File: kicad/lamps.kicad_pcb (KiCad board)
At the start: 2 copper layers, 30.5 x 31.8 mm, 24 parts, among them J1 BARREL_JACK, J2 Screw_Terminal_1x04, J3 Screw_Terminal_1x04, J4 CONN_01X05, Q1 NMOS-PMOS-SOT23-6, Q2 NMOS-PMOS-SOT23-6, Q3 NMOS-PMOS-SOT23-6, Q4 NMOS-PMOS-SOT23-6, Q5 NMOS-PMOS-SOT23-6, Q6 NMOS-PMOS-SOT23-6, U1 ESP-12E, U2 LD1117S33CTR

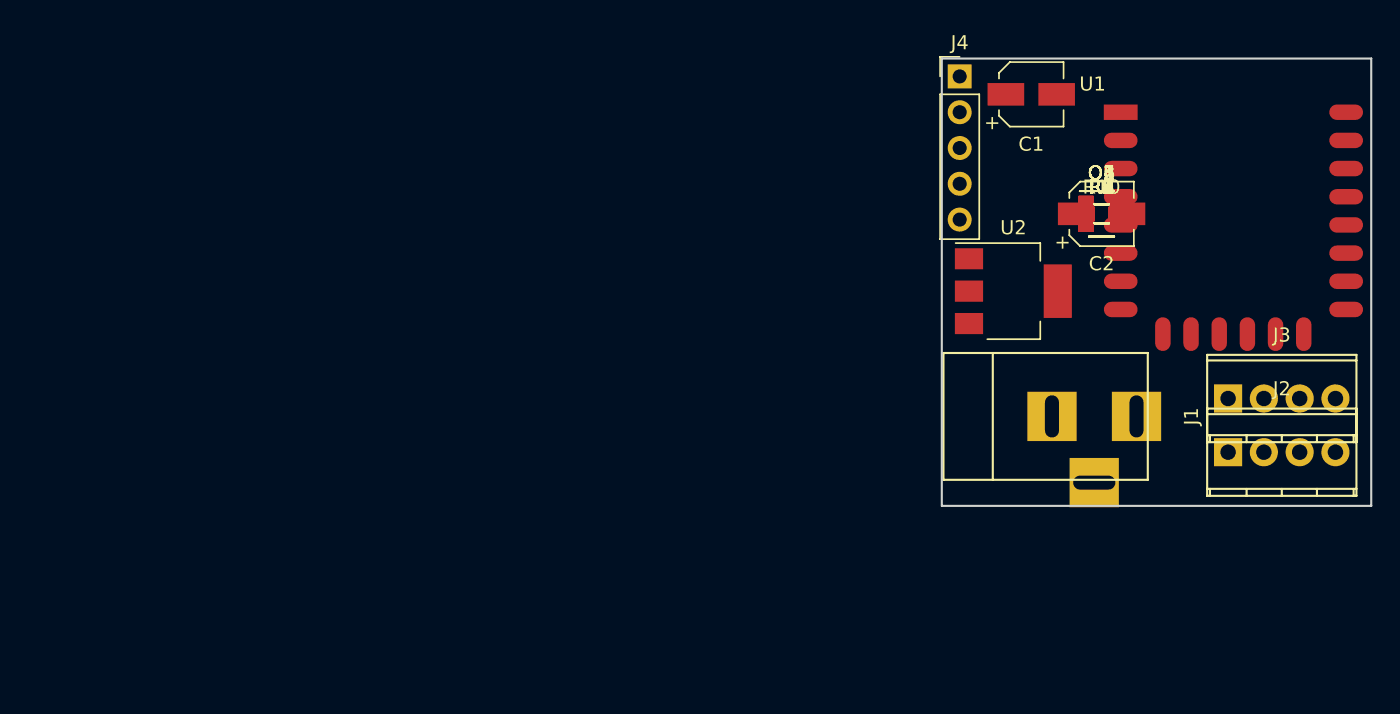
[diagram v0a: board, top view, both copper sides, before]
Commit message: start the pcb - the current layout pdf is definitely not the way Im going
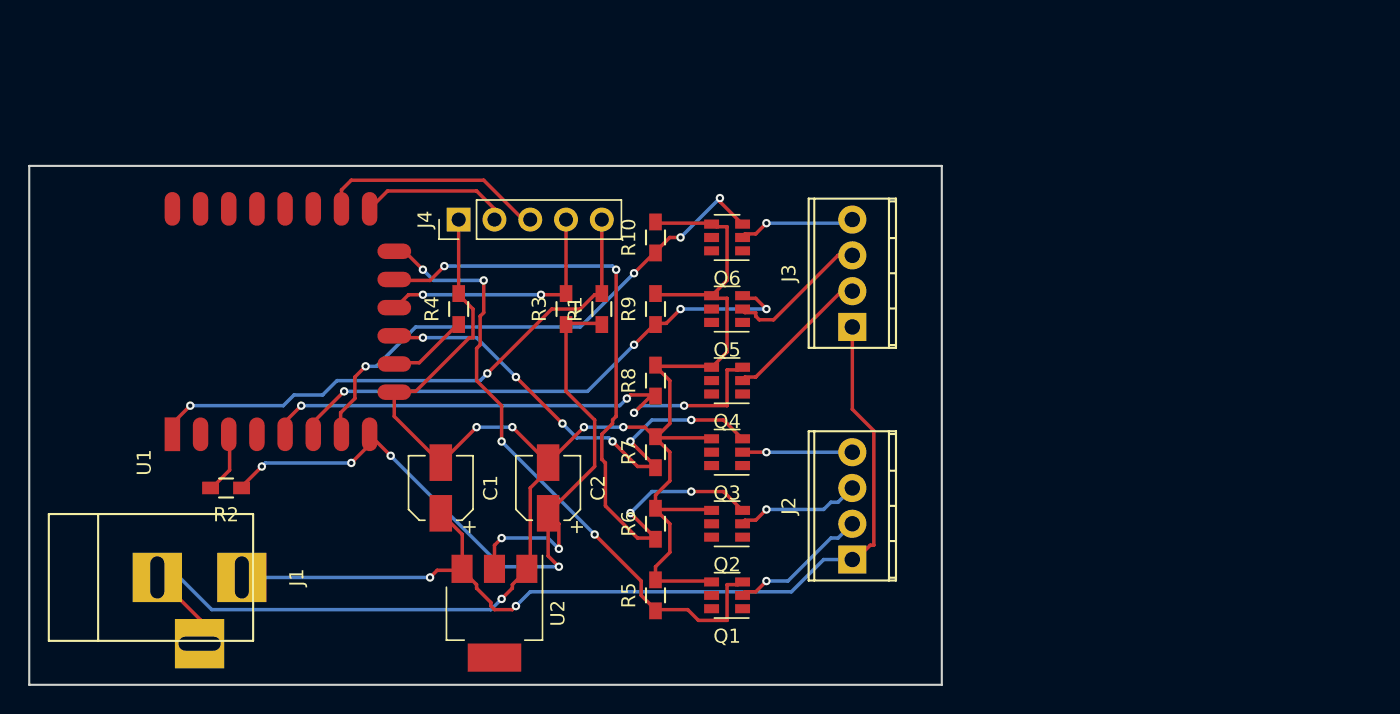
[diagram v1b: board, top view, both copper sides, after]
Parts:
- moved U1 71.1 mm to (82.5, 119.4), turned to 90 degrees
- moved R2 65.1 mm to (86.4, 123.2), turned to 180 degrees
- moved J1 64.5 mm to (81.3, 129.5)
- moved C1 50.4 mm to (101.6, 123.2), turned to 90 degrees
- moved R4 46.1 mm to (102.9, 110.5), turned to 90 degrees
- moved C2 43.8 mm to (109.2, 123.2), turned to 90 degrees
- moved U2 43.3 mm to (105.4, 132.1), turned to 270 degrees
- moved R5 41.7 mm to (116.8, 130.8), turned to 90 degrees
- moved R3 38.6 mm to (110.5, 110.5), turned to 90 degrees
- moved R6 38.6 mm to (116.8, 125.7), turned to 90 degrees
- moved Q1 37.9 mm to (121.9, 130.8), turned to 180 degrees
- moved J4 37.0 mm to (102.9, 104.1), turned to 90 degrees
- moved R1 36.1 mm to (113.0, 110.5), turned to 90 degrees
- moved R7 35.9 mm to (116.8, 120.7), turned to 90 degrees
- moved Q2 34.5 mm to (121.9, 125.7), turned to 180 degrees
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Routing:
- net GND: track 0.00 -> 141.3 mm, vias 0 -> 5
- net +12V: track 0.00 -> 69.6 mm, vias 0 -> 2
- net +3V3: track 0.00 -> 60.7 mm, vias 0 -> 6
- net /G1: track 0.00 -> 50.0 mm, vias 0 -> 4
- net /R1: track 0.00 -> 45.4 mm, vias 0 -> 4
- net /R2: track 0.00 -> 40.9 mm, vias 0 -> 4
- net /~Reset: track 0.00 -> 40.4 mm, vias 0 -> 2
- net /G2: track 0.00 -> 39.0 mm, vias 0 -> 4
- net /B2: track 0.00 -> 38.4 mm, vias 0 -> 4
- net /B1: track 0.00 -> 34.4 mm, vias 0 -> 6
- net /Prog: track 0.00 -> 18.0 mm, vias 0 -> 2
- net /TxD: track 0.00 -> 16.2 mm
- net /RxD: track 0.00 -> 10.7 mm
- net /LED2R: track 0.00 -> 10.6 mm
- net /LED2G: track 0.00 -> 10.3 mm
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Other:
- board size 30.5 x 31.8 mm -> 64.8 x 36.8 mm

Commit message: manual routing
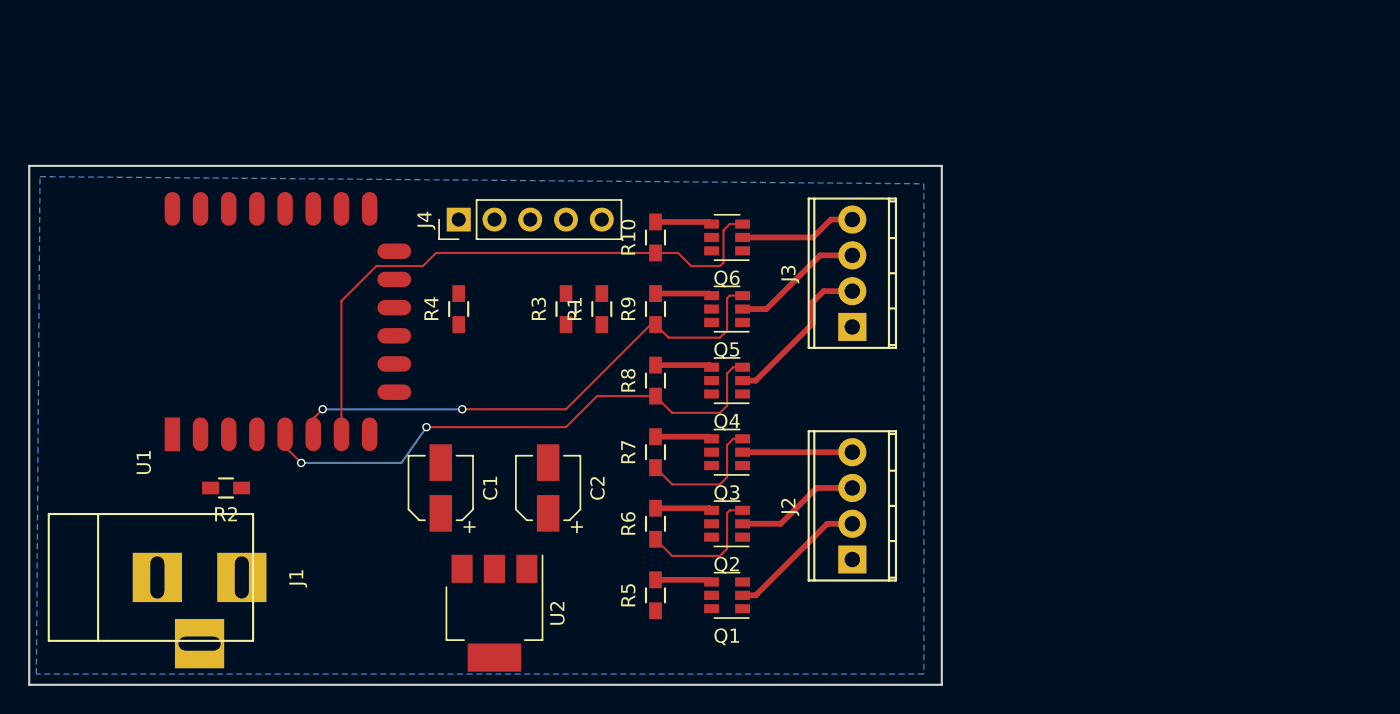
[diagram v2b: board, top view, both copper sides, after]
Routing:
- net GND: track 141.3 -> 24.3 mm, vias 5 -> 0
- net +12V: track 69.6 -> 0.00 mm, vias 2 -> 0
- net +3V3: track 60.7 -> 0.00 mm, vias 6 -> 0
- net /R1: track 45.4 -> 0.00 mm, vias 4 -> 0
- net /G1: track 50.0 -> 9.50 mm, vias 4 -> 0
- net /~Reset: track 40.4 -> 0.00 mm, vias 2 -> 0
- net /B1: track 34.4 -> 9.35 mm, vias 6 -> 0
- net /Prog: track 18.0 -> 0.00 mm, vias 2 -> 0
- net /TxD: track 16.2 -> 0.00 mm
- net /RxD: track 10.7 -> 0.00 mm
- net /GPIO15: track 5.90 -> 0.00 mm
- net /Enable: track 4.48 -> 0.00 mm
- net /B2: track 38.4 -> 42.3 mm, vias 4 -> 0
- net /R2: track 40.9 -> 39.2 mm, vias 4 -> 2
- net /G2: track 39.0 -> 37.3 mm, vias 4 -> 2
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- added copper zone on B.Cu, net GND
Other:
- net class Default: trace_width 0.25 -> 0.1524
- net class Power added: clearance 0.2, trace_width 0.4064, via_dia 0.6, via_drill 0.4
- rule trace_min: 0.2 -> 0.1524
